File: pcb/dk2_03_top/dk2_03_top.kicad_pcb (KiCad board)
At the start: 2 copper layers, 120 x 108 mm, 106 parts, among them J1 Conn_01x18_Pin, J10 Sync_Out, J11 Euro_Out_2, J12 CV_In_1, J13 CV_In_2, J14 CV_In_3, J15 CV_In_4, J2 Trigger_Out_1, J3 Trigger_Out_2, J4 Sync_In, J5 Euro_Out_1, J6 Micro_SD_Card, J7 Conn_01x18_Pin, J8 Trigger_Out_3, J9 Trigger_Out_4, SW1 SW_Push, SW10 SW_Push, SW11 SW_Push, SW12 SW_Push, SW13 SW_Push, SW14 SW_Push, SW15 SW_Push, SW16 SW_Push, SW17 SW_Push, SW18 SW_Push, SW2 SW_Push, SW3 SW_Push, SW4 SW_Push, SW5 SW_Push, SW6 SW_Push, SW7 SW_Push, SW8 SW_Push, SW9 SW_Push, U1 74HC595, U2 74HC595, U3 CA56-12EWA, U4 74HC165, U5 74HC165, U6 74HC4051, U7 MCP6002-xSN, U8 MCP6002-xSN, U9 74HC4051

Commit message: a commit before i mess up all the buttons
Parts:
- removed J7: Conn_01x18_Pin, Connector_PinHeader_2.54mm:PinHeader_1x18_P2.54mm_Vertical
- added J16: Conn_01x20_Socket, Connector_PinSocket_2.54mm:PinSocket_1x20_P2.54mm_Vertical, B.Cu at (74.0, 67.9)
- added J18: Conn_01x16_Socket, Connector_PinSocket_2.54mm:PinSocket_1x16_P2.54mm_Vertical, B.Cu at (186.0, 73.0)
- added R41: 10k, Resistor_SMD:R_0603_1608Metric, F.Cu at (249.7, 70.6)
- added R42: 10k, Resistor_SMD:R_0603_1608Metric, F.Cu at (249.7, 73.1)
- added R43: 10k, Resistor_SMD:R_0603_1608Metric, F.Cu at (249.7, 75.6)
- added SW19: SW_Push, Button_Switch_THT:SW_PUSH_6mm, F.Cu at (228.7, 88.5)
- added U10: 74HC165, Package_SO:SOIC-16_3.9x9.9mm_P1.27mm, B.Cu at (81.5, 106.6)
- J1: value Conn_01x18_Pin -> Conn_01x05_Pin; footprint Connector_PinHeader_2.54mm:PinHeader_1x18_P2.54mm_Vertical -> Connector_PinHeader_2.54mm:PinHeader_1x05_P2.54mm_Vertical; moved to F.Cu
- R1, R10, R11, R12, R2, R3, R4, R5, R6, R7, R8, R9: value 200R -> 75R
- SW1, SW2: footprint Button_Switch_THT:SW_PUSH-12mm -> Button_Switch_THT:SW_PUSH_6mm
- moved SW2 150.1 mm to (228.7, 79.9)
- moved SW1 149.3 mm to (228.7, 71.4)
- moved U5 11.1 mm to (81.5, 93.6)
- moved J1 8.06 mm to (66.0, 78.8), turned to 0 degrees
- moved U4 7.52 mm to (81.5, 81.6)
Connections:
- J1 pad 1: unconnected-(J1-Pin_1-Pad1) -> Net-(J1-Pin_1)
- J1 pad 2: unconnected-(J1-Pin_2-Pad2) -> Net-(J1-Pin_2)
- J1 pad 3: unconnected-(J1-Pin_3-Pad3) -> Net-(J1-Pin_3)
- J1 pad 4: START_STOP_BUTTON -> Net-(J1-Pin_4)
- J1 pad 5: TAP_TEMPO_BUTTON -> Net-(J1-Pin_5)
- SW1 pad 1: GND -> +3.3V
- SW1 pad 2: START_STOP_BUTTON -> Net-(U10-D0)
- SW2 pad 1: GND -> +3.3V
- SW2 pad 2: TAP_TEMPO_BUTTON -> Net-(U10-D1)
- U5 pad 9: 165_DATA -> /Shift register in 2/DATA_OUT
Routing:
- net TAP_TEMPO_BUTTON: track 37.6 -> 0.00 mm
- net 165_CLOCK: track 43.0 -> 67.7 mm
- net TRIGGER_OUT_3_EURO: track 53.8 -> 75.2 mm
- net START_STOP_BUTTON: track 20.4 -> 0.00 mm
- net unconnected-(U5-~{Q7}-Pad7): track 0.00 -> 16.3 mm
- net /Shift register in 1/DATA_OUT: track 16.3 -> 0.00 mm
- net 165_DATA: track 21.5 -> 37.6 mm
- net GND: track 213.7 -> 209.4 mm
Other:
- board text added: "Drumkid 2.03 (Eurorack)"
- board text removed: "Drumkid 2.02 (Eurorack)"

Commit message: routing top pcb
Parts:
- removed the SW12 at (107.0, 105.0)
- removed the SW13 at (117.0, 105.0)
- removed the SW4 at (107.0, 81.0)
- removed the SW5 at (117.0, 81.0)
- added SW1: SW_Push, Button_Switch_THT:SW_PUSH_6mm, F.Cu at (87.0, 81.0)
- added SW10: SW_Push, Button_Switch_THT:SW_PUSH_6mm, F.Cu at (127.0, 93.0)
- added SW2: SW_Push, Button_Switch_THT:SW_PUSH_6mm, F.Cu at (97.0, 81.0)
- added SW9: SW_Push, Button_Switch_THT:SW_PUSH_6mm, F.Cu at (117.0, 93.0)
- R41, R42, R43: moved to B.Cu
- moved R41 102.1 mm to (155.2, 109.0), turned to 180 degrees
- moved R42 91.9 mm to (165.2, 109.0), turned to 180 degrees
- moved SW17 83.7 mm to (152.0, 105.0)
- moved R43 81.9 mm to (175.0, 109.0), turned to 180 degrees
- moved SW18 71.2 mm to (162.0, 105.0)
- moved SW19 59.0 mm to (172.0, 105.0)
- moved J16 56.6 mm to (74.0, 134.9)
- moved SW13 35.0 mm to (107.0, 105.0)
- moved SW14 35.0 mm to (117.0, 105.0)
- moved SW15 35.0 mm to (127.0, 105.0)
- moved R25 32.4 mm to (110.2, 109.0)
- moved R26 32.4 mm to (120.2, 109.0)
- moved R27 32.4 mm to (130.2, 109.0)
- moved R17 32.3 mm to (130.2, 85.0)
- moved SW5 32.3 mm to (127.0, 81.0)
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- renumbered J16 to J1, J1 to J16, J18 to J7, R7 to R10, R8 to R11, R10 to R12, R9 to R5, R11 to R6, R12 to R7, R5 to R8, R6 to R9, SW14 to SW12, SW15 to SW13, SW16 to SW14, SW17 to SW15, SW18 to SW16, SW1 to SW17, SW2 to SW18, SW6 to SW4, SW7 to SW5, SW8 to SW6, SW9 to SW7, SW10 to SW8
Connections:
- SW11 pad 2: Net-(U5-D0) -> Net-(U5-D2)
- SW3 pad 2: Net-(U4-D0) -> Net-(U4-D2)
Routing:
- net GND: track 209.4 -> 62.4 mm, vias 13 -> 7
- net Net-(U10-D2): track 0.00 -> 119.8 mm, vias 0 -> 1
- net +3.3V: track 586.9 -> 474.8 mm, vias 8 -> 5
- net Net-(U10-D1): track 0.00 -> 103.5 mm, vias 0 -> 1
- net Net-(U10-D0): track 0.00 -> 90.6 mm, vias 0 -> 1
- net TRIGGER_OUT_3_EURO: track 75.2 -> 0.00 mm
- net 4051_READING_1: track 43.3 -> 117.7 mm, vias 1 -> 2
- net 4051_ADDRESS_C: track 53.4 -> 127.0 mm
- net 4051_READING_0: track 73.9 -> 0.38 mm, vias 1 -> 0
- net 4051_ADDRESS_B: track 54.1 -> 126.5 mm
- net 4051_ADDRESS_A: track 54.0 -> 124.1 mm
- net CV_IN_1: track 105.0 -> 43.8 mm
- net TRIGGER_OUT_2_EURO: track 54.3 -> 0.00 mm
- net Net-(U5-D3): track 63.3 -> 10.0 mm, vias 1 -> 0
- net TRIGGER_OUT_4_EURO: track 46.4 -> 0.00 mm, vias 1 -> 0
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
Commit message: top pcb routed
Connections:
- J1 pad 16: +12V -> unconnected-(J1-Pin_16-Pad16)
- J1 pad 17: +3.3VDAC -> unconnected-(J1-Pin_17-Pad17)
- J1 pad 20: -12V -> unconnected-(J1-Pin_20-Pad20)
- J7 pad 13: +3.3VDAC -> unconnected-(J7-Pin_13-Pad13)
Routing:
- net GND: track 62.4 -> 340.3 mm, vias 7 -> 14
- net +3.3V: track 474.8 -> 676.9 mm, vias 5 -> 9
- net 4051_READING_0: track 0.38 -> 107.1 mm, vias 0 -> 2
- net TRIGGER_OUT_4_EURO: track 0.00 -> 65.1 mm
- net CV_IN_1: track 43.8 -> 106.4 mm
- net SYNC_OUT_EURO: track 0.00 -> 62.4 mm
- net Net-(U5-D1): track 10.0 -> 67.8 mm, vias 0 -> 2
- net TRIGGER_OUT_2_EURO: track 0.00 -> 57.6 mm
- net TRIGGER_OUT_3_EURO: track 0.00 -> 52.8 mm
- net TRIGGER_OUT_1_EURO: track 0.00 -> 47.3 mm
- net Net-(U5-D0): track 10.0 -> 54.9 mm, vias 0 -> 2
- net SYNC_IN_EURO: track 0.00 -> 39.4 mm, vias 0 -> 2
- net Net-(U5-D3): track 10.0 -> 43.8 mm, vias 0 -> 1
- net Net-(J16-Pin_1): track 3.56 -> 33.3 mm
- net Net-(U5-D2): track 10.0 -> 37.8 mm, vias 0 -> 1
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
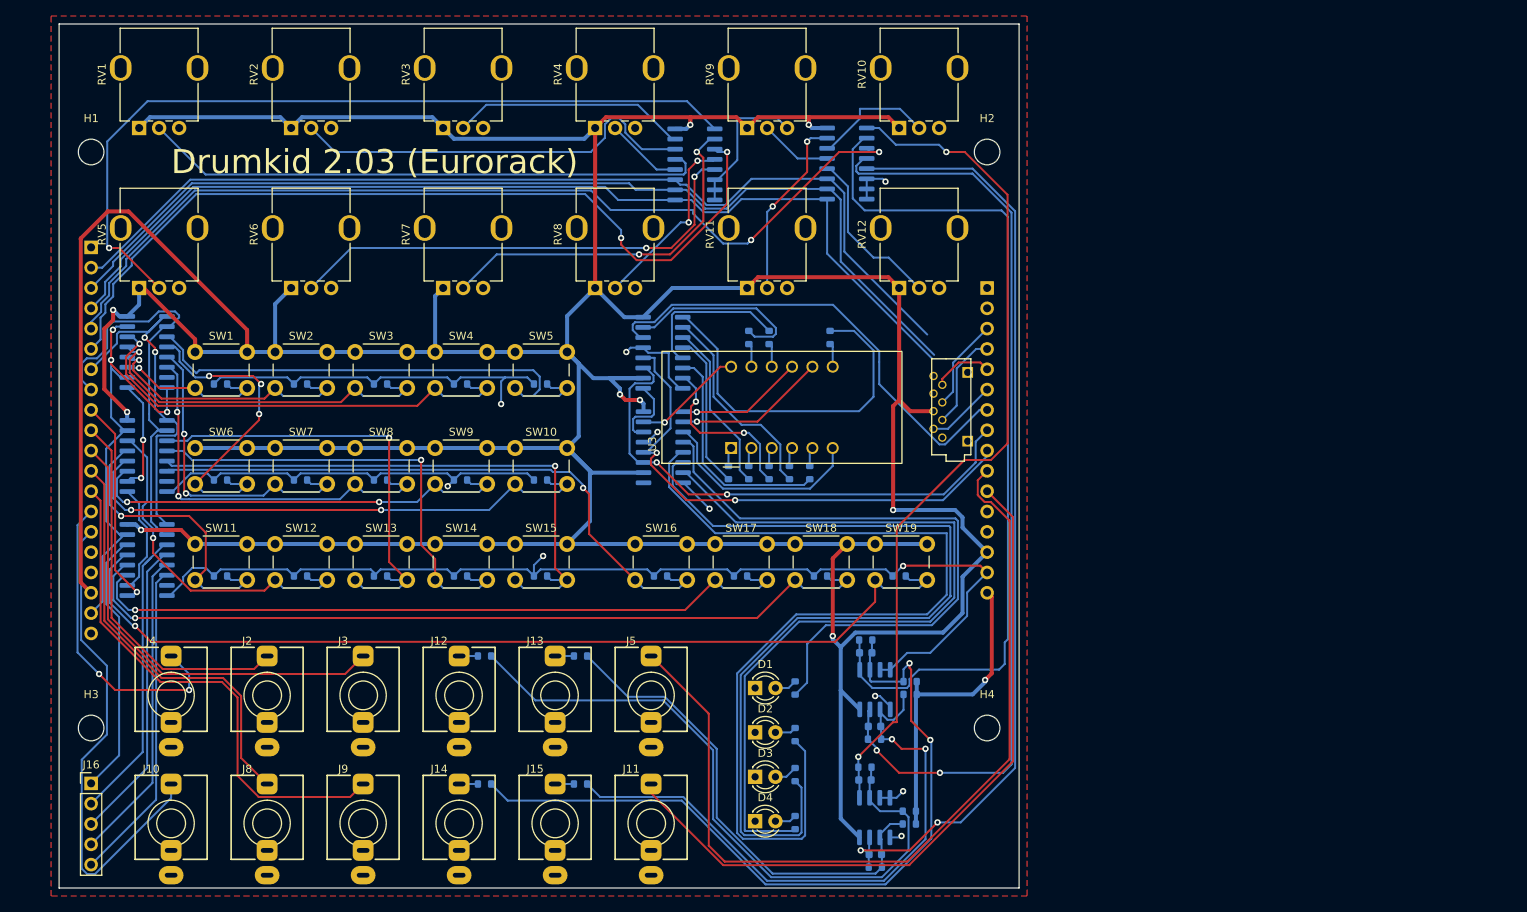
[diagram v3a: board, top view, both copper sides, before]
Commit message: routing bottom pcb
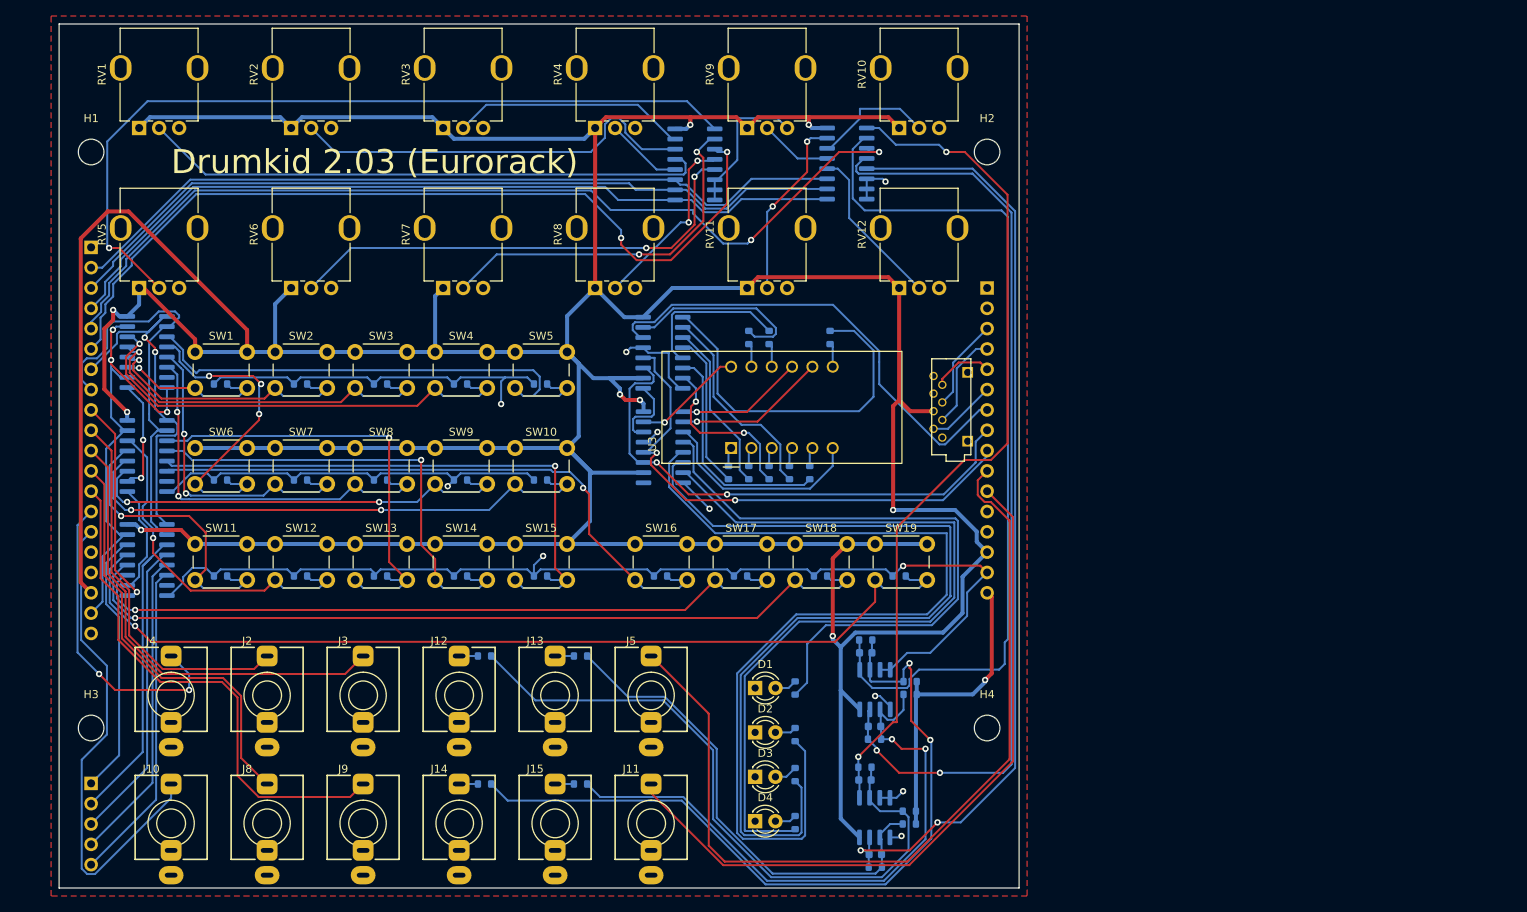
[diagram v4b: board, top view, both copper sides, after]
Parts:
- J16: moved to B.Cu
- turned J16 to 180 degrees
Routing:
- net 4051_ADDRESS_B: track 126.5 -> 100.0 mm
- net 4051_ADDRESS_C: track 127.0 -> 101.7 mm
- net 4051_ADDRESS_A: track 124.1 -> 99.2 mm
- net +3.3V: track 676.9 -> 674.9 mm
- net 165_LOAD: track 45.7 -> 44.5 mm
- net Net-(U9-A3): track 21.0 -> 20.5 mm

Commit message: fixed an issue where i forgot to rotate the pots on the pcb
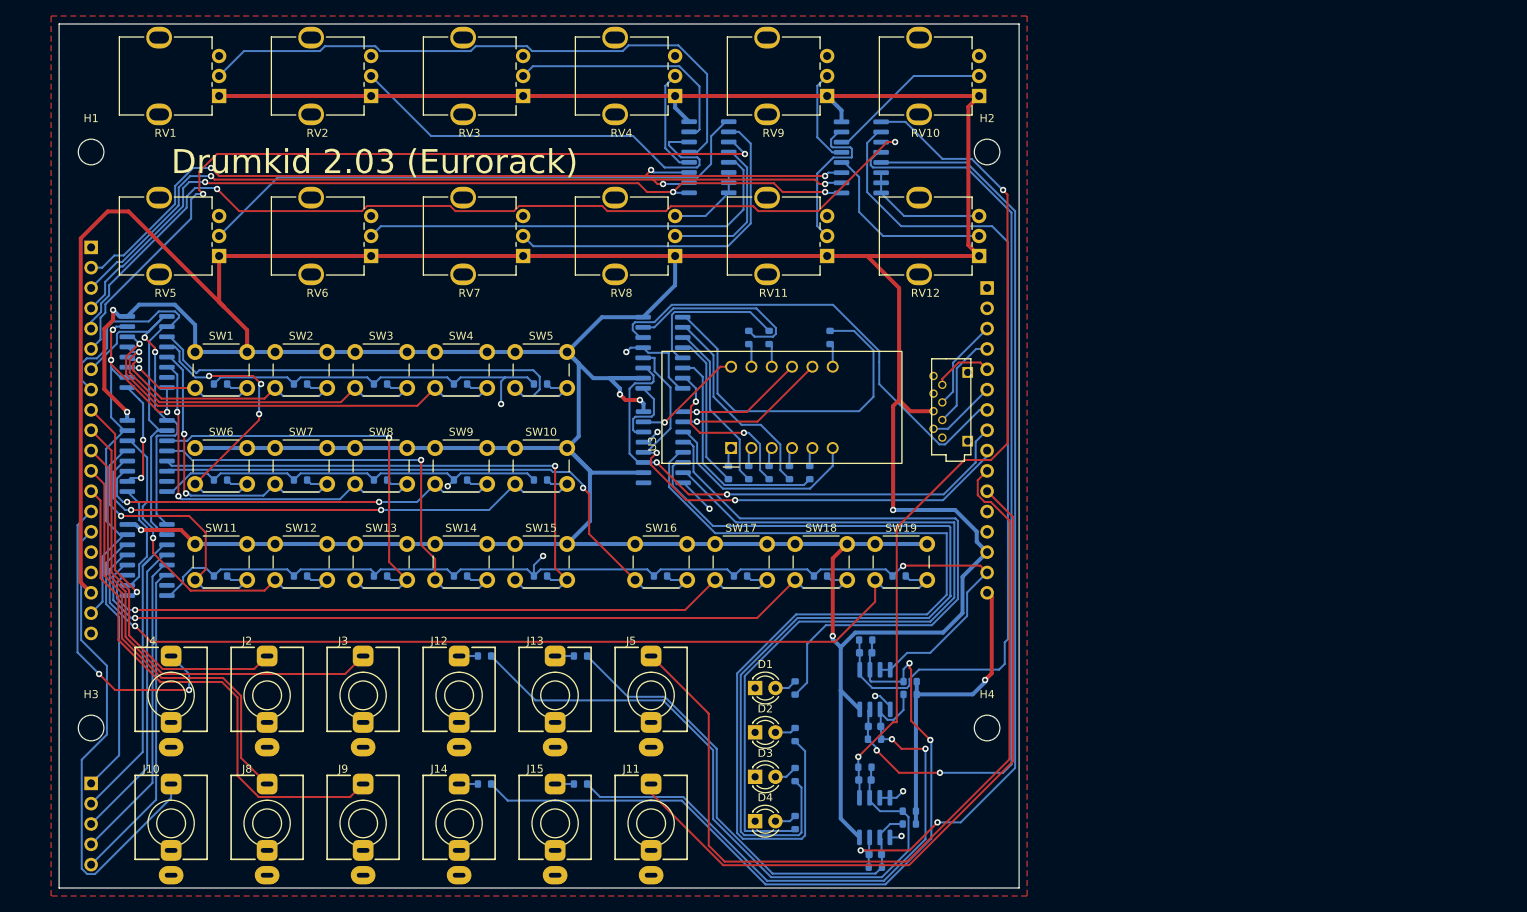
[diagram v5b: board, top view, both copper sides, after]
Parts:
- moved RV1 10.8 mm to (90.0, 49.0), turned to 180 degrees
- moved RV10 10.8 mm to (185.0, 49.0), turned to 180 degrees
- moved RV11 10.8 mm to (166.0, 69.0), turned to 180 degrees
- moved RV12 10.8 mm to (185.0, 69.0), turned to 180 degrees
- moved RV2 10.8 mm to (109.0, 49.0), turned to 180 degrees
- moved RV3 10.8 mm to (128.0, 49.0), turned to 180 degrees
- moved RV4 10.8 mm to (147.0, 49.0), turned to 180 degrees
- moved RV5 10.8 mm to (90.0, 69.0), turned to 180 degrees
- moved RV6 10.8 mm to (109.0, 69.0), turned to 180 degrees
- moved RV7 10.8 mm to (128.0, 69.0), turned to 180 degrees
- moved RV8 10.8 mm to (147.0, 69.0), turned to 180 degrees
- moved RV9 10.8 mm to (166.0, 49.0), turned to 180 degrees
- moved U6 1.97 mm to (151.2, 56.7)
- moved U9 1.96 mm to (170.3, 56.7)
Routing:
- net +3.3V: track 674.9 -> 734.0 mm, vias 9 -> 7
- net Net-(U6-A4): track 101.2 -> 71.6 mm, vias 1 -> 0
- net 4051_ADDRESS_A: track 99.2 -> 107.1 mm, vias 0 -> 3
- net 4051_READING_0: track 106.7 -> 100.4 mm
- net 4051_ADDRESS_B: track 100.0 -> 106.2 mm, vias 0 -> 3
- net Net-(U9-A1): track 15.3 -> 20.6 mm
- net Net-(U6-A0): track 71.0 -> 76.3 mm
- net Net-(U6-A5): track 60.1 -> 55.1 mm, vias 2 -> 0
- net 4051_ADDRESS_C: track 101.7 -> 106.1 mm, vias 0 -> 3
- net Net-(U6-A7): track 23.4 -> 19.6 mm, vias 2 -> 0
- net Net-(U6-A3): track 9.65 -> 13.2 mm
- net CV_IN_3: track 109.8 -> 106.5 mm
- net Net-(U9-A2): track 23.0 -> 19.8 mm, vias 2 -> 0
- net GND: track 340.3 -> 343.4 mm, vias 14 -> 13
- net Net-(U9-A3): track 20.5 -> 23.6 mm
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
